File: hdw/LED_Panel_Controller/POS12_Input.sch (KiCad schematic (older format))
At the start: 21 parts

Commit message: made a lot more schematic progress
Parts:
- removed FL?: DLW5ATN501MQ2L, symbol Custom_Library:DLW5ATN501MQ2L
- removed R?: 1.15k, Resistors_SMD:R_0402, symbol Custom_Library:R_Custom
- removed R?: 51.1k, Resistors_SMD:R_0402, symbol Custom_Library:R_Custom
- removed R? (x3): 5.11k, Resistors_SMD:R_0402, symbol Custom_Library:R_Custom
- removed R?: 13k, Resistors_SMD:R_0402, symbol Custom_Library:R_Custom
- added R? (x7): 10k, Resistors_SMD:R_0402, symbol Custom_Library:R_Custom
- added R? (x4): 1k, Resistors_SMD:R_0402, symbol Custom_Library:R_Custom
- added R? (x2): 100k, Resistors_SMD:R_0402, symbol Custom_Library:R_Custom
- added R? (x3): 0, Resistors_SMD:R_0402, symbol Custom_Library:R_Custom
- C?: footprint (none) -> Capacitors_SMD:C_0402; Digi-Key PN (none) -> 490-10698-1-ND; Voltage 50V -> 25V
- C?: footprint (none) -> Capacitors_SMD:C_0402; Digi-Key PN (none) -> 399-3066-1-ND
- D?: Configuration (none) -> DNP
- R? (x2): Digi-Key PN (none) -> RMCF0402FT10K0CT-ND
- R?: Configuration (none) -> Telemetry
- R? (x2): Configuration (none) -> Telemetry; Digi-Key PN (none) -> RMCF0402FT10R0CT-ND
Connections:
- wire segments 70 -> 92
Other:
- note added: "UVLO threshold set to 11.12V\nOVLO threshold set to 13.33V\n\nMODE set to Circuit Breaker with Auto-Retry\n\nOutput Current Limit set to 1.2A\n\nOutput ramp rate = 12.5V/ms"
- note removed: "UVLO threshold set to 10.8V\nOVLO threshold set to 13.2V\n\nMODE set to Circuit Breaker with Auto-Retry\n\nOutput Current Limit set to 2A"
- moved on the sheet: C?, D?, J?, R?, TP?, U?

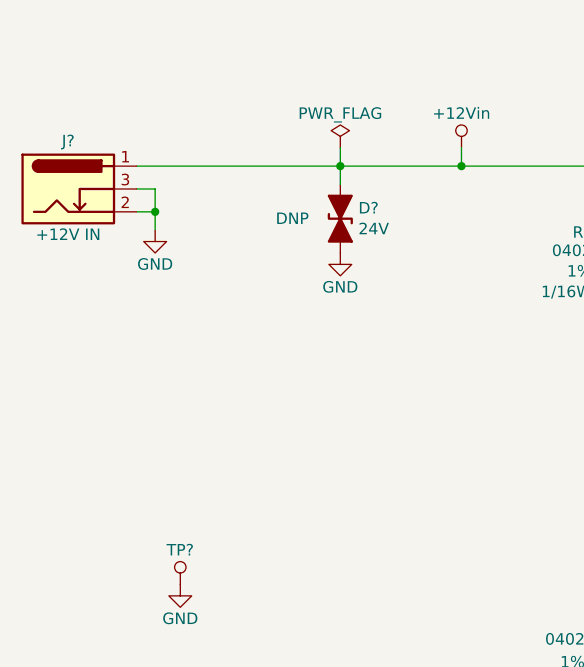
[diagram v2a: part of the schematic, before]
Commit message: fixed level shifter sheet
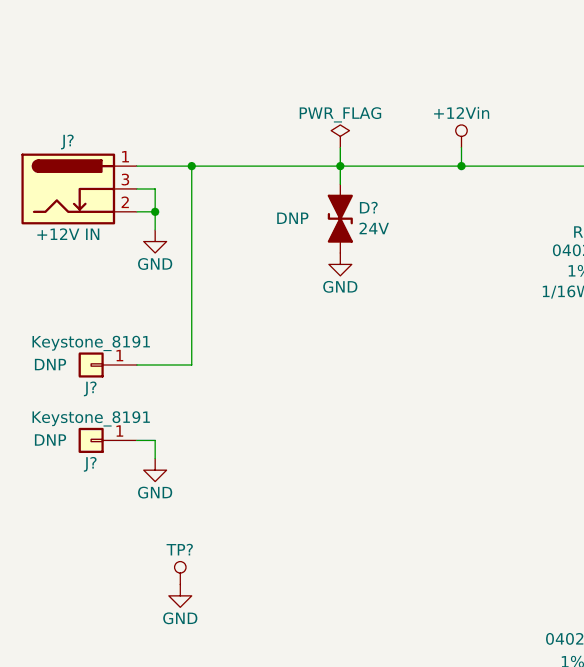
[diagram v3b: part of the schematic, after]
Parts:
- added J? (x2): Keystone_8191, Custom Footprints Library:Keystone_8191, symbol Connector_Generic:Conn_01x01
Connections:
- net +12Vin: now also J?.1 (Pin_1)
- net GND: now also J?.1 (Pin_1)
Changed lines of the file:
@@
 Connection ~ 2010 2440
 Wire Wire Line
-	1930 2240 2820 2240
+	1930 2240 2170 2240
 Text Notes 2050 5570 0    50   ~ 0
 UVLO threshold set to 11.12V\nOVLO threshold set to 13.33V\n\nMODE set to Circuit Breaker with Auto-Retry\n\nOutput Current Limit set to 1.2A\n\nOutput ramp rate = 12.5V/ms
@@
 Wire Wire Line
 	6900 4840 8640 4840
+Wire Wire Line
+	1930 3110 2170 3110
+Wire Wire Line
+	2170 3110 2170 2240
+Connection ~ 2170 2240
+Wire Wire Line
+	2170 2240 2820 2240
+$Comp
+L power:GND #PWR?
+U 1 1 601820E0
+P 2010 3520
+F 0 "#PWR?" H 2010 3270 50  0001 C CNN
+F 1 "GND" H 2010 3370 50  0000 C CNN
+F 2 "" H 2010 3520 50  0001 C CNN
+F 3 "" H 2010 3520 50  0001 C CNN
+	1    2010 3520
+	1    0    0    -1
+$EndComp
+Wire Wire Line
+	2010 3520 2010 3440
+Wire Wire Line
+	2010 3440 1930 3440
+$Comp
+L Connector_Generic:Conn_01x01 J?
+U 1 1 6017C82A
+P 1730 3110
+F 0 "J?" H 1730 3210 50  0000 C CNN
+F 1 "Keystone_8191" H 1730 3010 50  0000 C CNN
+F 2 "Custom Footprints Library:Keystone_8191" H 1730 3110 50  0001 C CNN
+F 3 "~" H 1730 3110 50  0001 C CNN
+F 4 "DNP" H 1910 3110 50  0000 C CNN "Configuration"
+	1    1730 3110
+	-1   0    0    1
+$EndComp
+$Comp
+L Connector_Generic:Conn_01x01 J?
+U 1 1 60188AA9
+P 1730 3440
+F 0 "J?" H 1730 3540 50  0000 C CNN
+F 1 "Keystone_8191" H 1730 3340 50  0000 C CNN
+F 2 "Custom Footprints Library:Keystone_8191" H 1730 3440 50  0001 C CNN
+F 3 "~" H 1730 3440 50  0001 C CNN
+F 4 "DNP" H 1910 3440 50  0000 C CNN "Configuration"
+	1    1730 3440
+	-1   0    0    1
+$EndComp
 $EndSCHEMATC

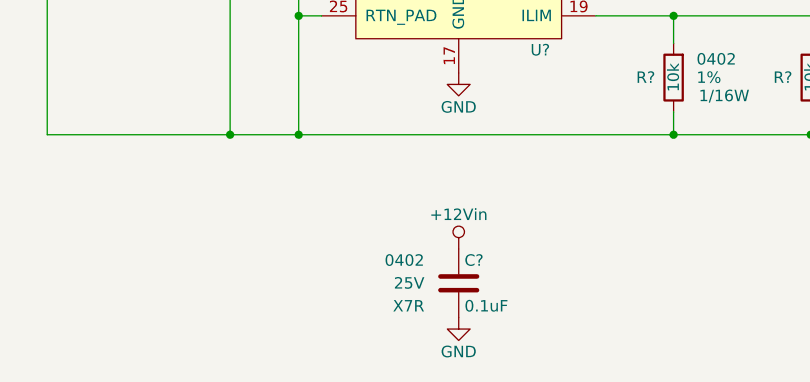
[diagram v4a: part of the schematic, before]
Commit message: added digikey pns, footprints, bom scrubbed
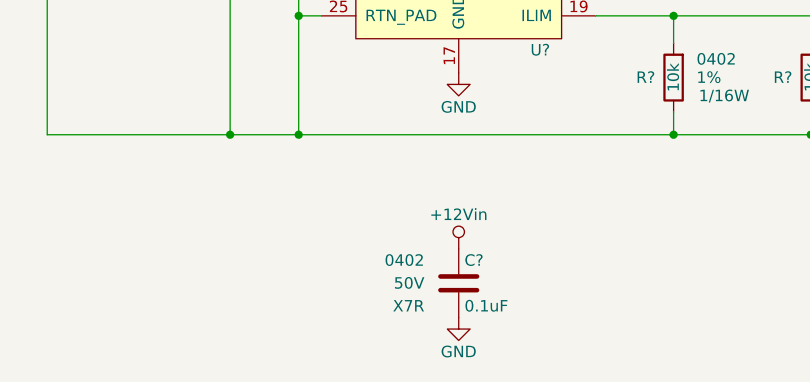
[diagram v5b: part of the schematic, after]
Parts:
- C?: Digi-Key PN 490-10698-1-ND -> 490-10701-1-ND; Voltage 25V -> 50V
- J? (x2): Digi-Key PN (none) -> 36-8191-ND
- R? (x3): Digi-Key PN 2019-RK73Z1ETTPCT-ND -> RMCF0402ZT0R00CT-ND
- TP? (x2): value TP_Pad -> TP
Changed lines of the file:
@@
 F 3 "" H 6325 6210 50  0001 C CNN
 F 4 "0402" H 6150 6210 50  0000 R CNN "display_footprint"
-F 5 "25V" H 6150 6110 50  0000 R CNN "Voltage"
+F 5 "50V" H 6150 6110 50  0000 R CNN "Voltage"
 F 6 "X7R" H 6150 6010 50  0000 R CNN "Dielectric"
-F 7 "490-10698-1-ND" H 6725 6610 60  0001 C CNN "Digi-Key PN"
+F 7 "490-10701-1-ND" H 6725 6610 60  0001 C CNN "Digi-Key PN"
 	1    6300 6110
 	1    0    0    -1
@@
 P 7910 2170
 F 0 "TP?" H 7910 2320 50  0000 C CNN
-F 1 "TP_Pad" H 7910 2320 50  0001 C CNN
+F 1 "TP" H 7910 2320 50  0001 C CNN
 F 2 "Custom Footprints Library:Test_Point" H 7910 2170 60  0001 C CNN
 F 3 "" H 7910 2170 60  0000 C CNN
@@
 P 4500 2160
 F 0 "TP?" H 4500 2310 50  0000 C CNN
-F 1 "TP_Pad" H 4500 2310 50  0001 C CNN
+F 1 "TP" H 4500 2310 50  0001 C CNN
 F 2 "Custom Footprints Library:Test_Point" H 4500 2160 60  0001 C CNN
 F 3 "" H 4500 2160 60  0000 C CNN
@@
 F 6 "1/16W" V 7510 2640 50  0001 C CNN "Wattage"
 F 7 "~Telemetry" V 7310 2640 50  0000 C CNN "Configuration"
-F 8 "2019-RK73Z1ETTPCT-ND" H 7210 2640 50  0001 C CNN "Digi-Key PN"
+F 8 "RMCF0402ZT0R00CT-ND" H 7210 2640 50  0001 C CNN "Digi-Key PN"
 	1    7210 2640
 	0    -1   1    0
@@
 F 6 "1/16W" V 7510 2940 50  0001 C CNN "Wattage"
 F 7 "~Telemetry" V 7310 2940 50  0000 C CNN "Configuration"
-F 8 "2019-RK73Z1ETTPCT-ND" H 7210 2940 50  0001 C CNN "Digi-Key PN"
+F 8 "RMCF0402ZT0R00CT-ND" H 7210 2940 50  0001 C CNN "Digi-Key PN"
 	1    7210 2940
 	0    -1   1    0
@@
 F 6 "1/16W" V 7510 3240 50  0001 C CNN "Wattage"
 F 7 "~Telemetry" V 7310 3240 50  0000 C CNN "Configuration"
-F 8 "2019-RK73Z1ETTPCT-ND" H 7210 3240 50  0001 C CNN "Digi-Key PN"
+F 8 "RMCF0402ZT0R00CT-ND" H 7210 3240 50  0001 C CNN "Digi-Key PN"
 	1    7210 3240
 	0    -1   1    0
@@
 F 3 "~" H 1730 3110 50  0001 C CNN
 F 4 "DNP" H 1910 3110 50  0000 C CNN "Configuration"
+F 5 "36-8191-ND" H 1730 3110 50  0001 C CNN "Digi-Key PN"
 	1    1730 3110
 	-1   0    0    1
@@
 F 3 "~" H 1730 3440 50  0001 C CNN
 F 4 "DNP" H 1910 3440 50  0000 C CNN "Configuration"
+F 5 "36-8191-ND" H 1730 3440 50  0001 C CNN "Digi-Key PN"
 	1    1730 3440
 	-1   0    0    1

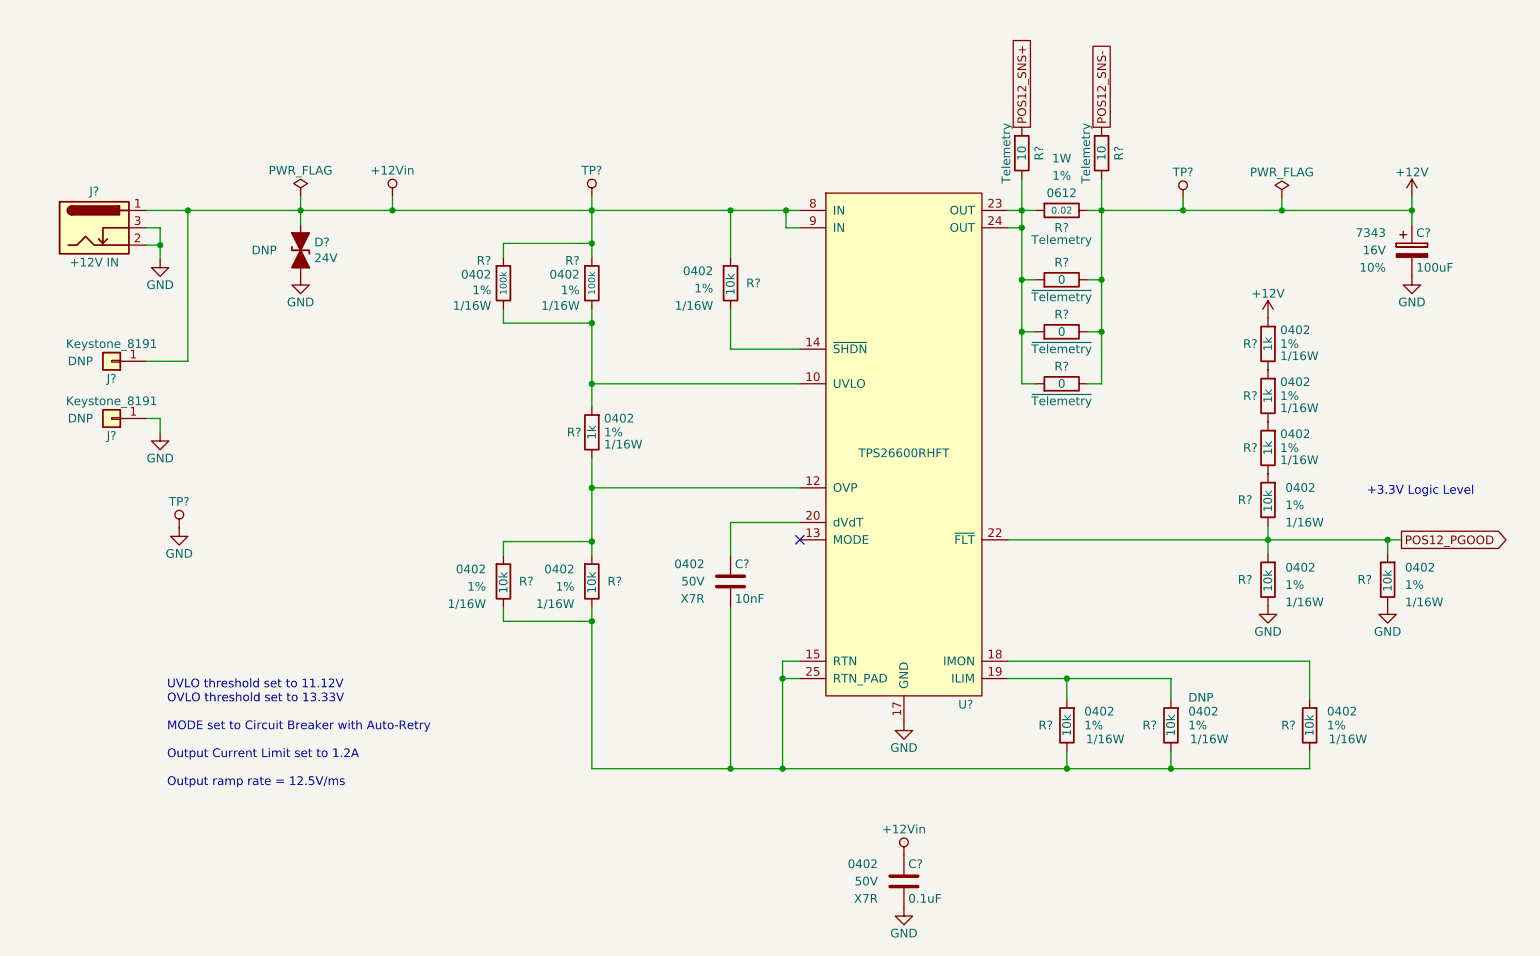
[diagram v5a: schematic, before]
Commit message: assigned I2C addresses
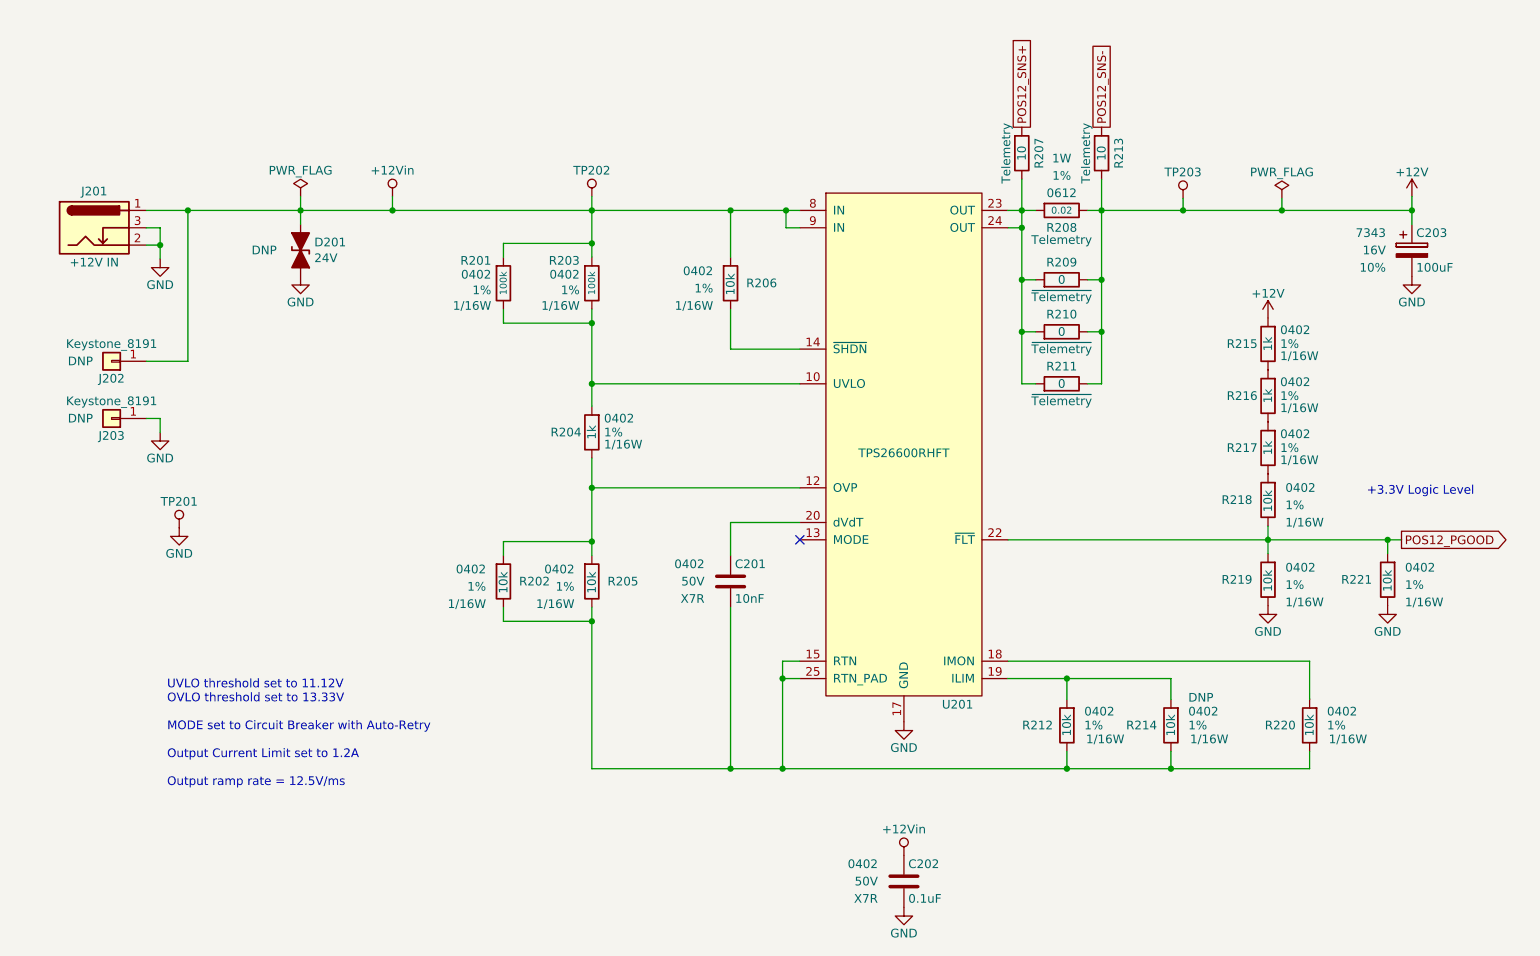
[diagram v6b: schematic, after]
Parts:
- gave numbers to parts that had none: 32
